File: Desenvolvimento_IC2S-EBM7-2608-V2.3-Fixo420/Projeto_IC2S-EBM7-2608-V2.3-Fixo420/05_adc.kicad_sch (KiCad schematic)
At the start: 17 parts, among them T7 TP_GND_ADC, U6 AD7124-8BCPZ, U7 ADR4525BRZ

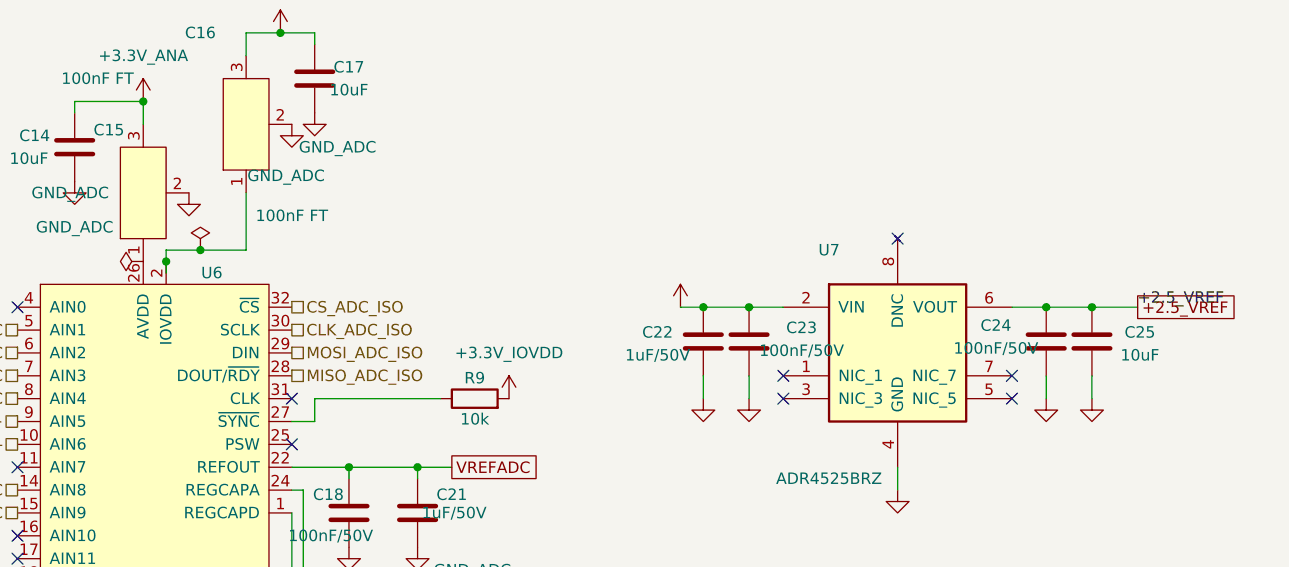
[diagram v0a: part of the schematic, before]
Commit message: Limpeza do ERC/DRC: fio solto e rotulo duplicado na folha 5, notas do C1 na folha 2, texto do C35
- 05_adc: removido o troco de fio de 1,27 mm em (128,27; 78,74)-(128,27; 80,01)
  com a junction que so existia por ele (extremo sem ligacao no ERC), e o
  rotulo local +2.5_VREF sobreposto ao global em (236,22; 83,82).
- 02_entrada: notas 4 e 12 falavam de "C1/C13" da numeracao antiga; o C13 e
  hoje o bypass do VCC2 do U5. A entrada do U1 (R-78HB) e o C1.
- PCB: texto de serigrafia ${REFERENCE} do C35 afastado do pad do C36.

Netlist do kicad-cli identica pino a pino antes/depois (104 redes;
+2.5_VREF = C24, C25, R8, U6.20, U7.6). DRC com paridade: 0 erros, 0 avisos,
0 desligados, paridade 0. Pacote de fabricacao regenerado.

Co-Authored-By: Claude Opus 5.5 (1M context) <noreply@anthropic.com>
Claude-Session: https://claude.ai/code/session_01KPnkiJQKrkjgRqqw9M78ie
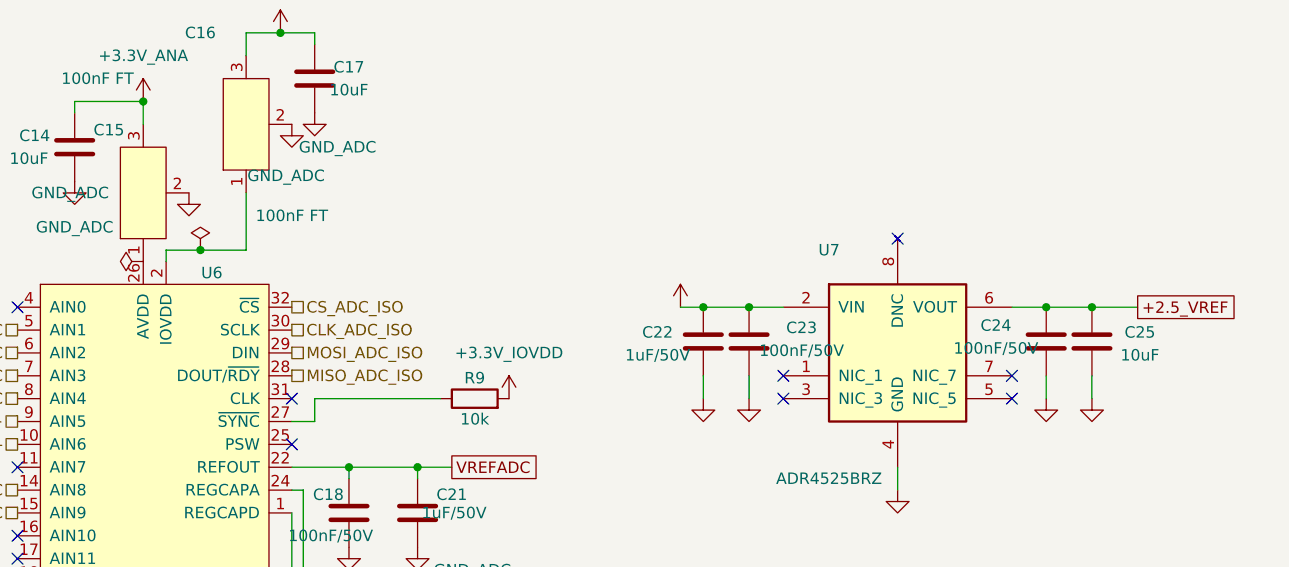
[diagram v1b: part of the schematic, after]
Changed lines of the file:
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@@
 		(color 0 0 0 0)
 	)
-	(junction
-		(at 128.27 78.74)
-		(diameter 0)
-		(color 0 0 0 0)
-	)
 	(no_connect
 		(at 111.76 111.76)
@@
 		(pts
 			(xy 140.97 53.34) (xy 144.78 53.34)
-		)
-		(stroke
-			(width 0)
-			(type default)
-		)
-	)
-	(wire
-		(pts
-			(xy 128.27 80.01) (xy 128.27 78.74)
 		)
 		(stroke
@@
 		)
 	)
-	(label "+2.5_VREF"
-		(at 236.22 83.82 0)
-		(effects
-			(font
-				(size 1.27 1.27)
-			)
-			(justify left bottom)
-		)
-	)
